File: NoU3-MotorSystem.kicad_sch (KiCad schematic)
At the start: 38 parts, among them J1 JST SR/SZ, J10 JST SR/SZ, J13 JST SR/SZ, J15 Barrel_Jack, J16 VIN, J17 JST SR/SZ, J18 GND, J4 JST SR/SZ, J7 JST SR/SZ, Q1 AO3401A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

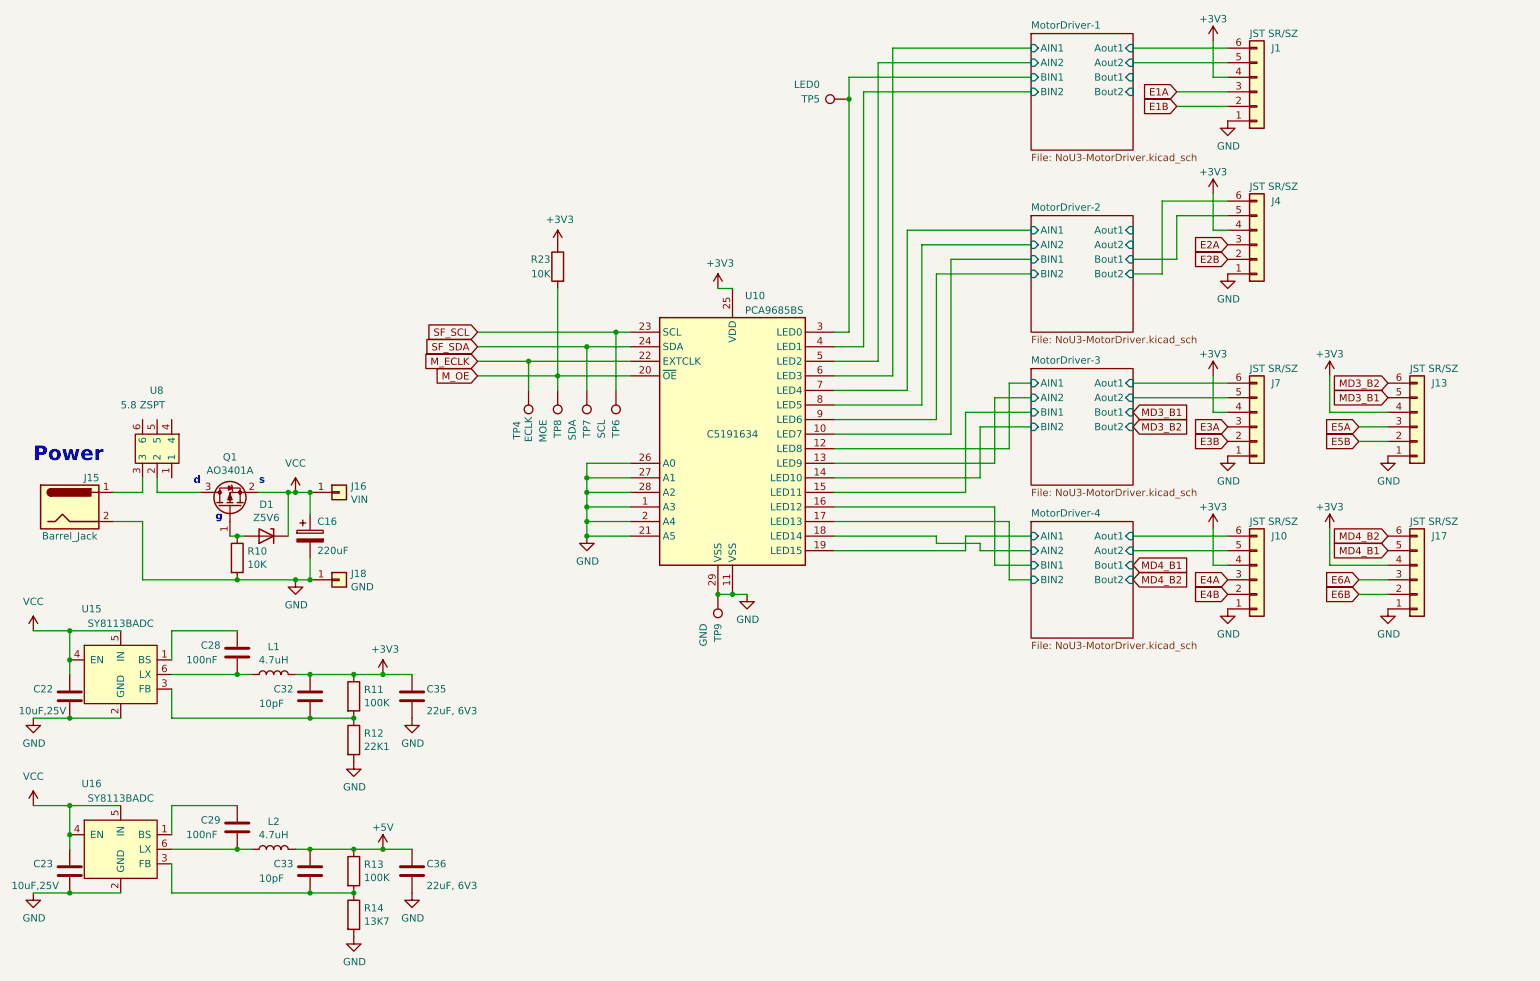
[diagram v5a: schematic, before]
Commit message: added 7th encoder, 2nd 220uf cap
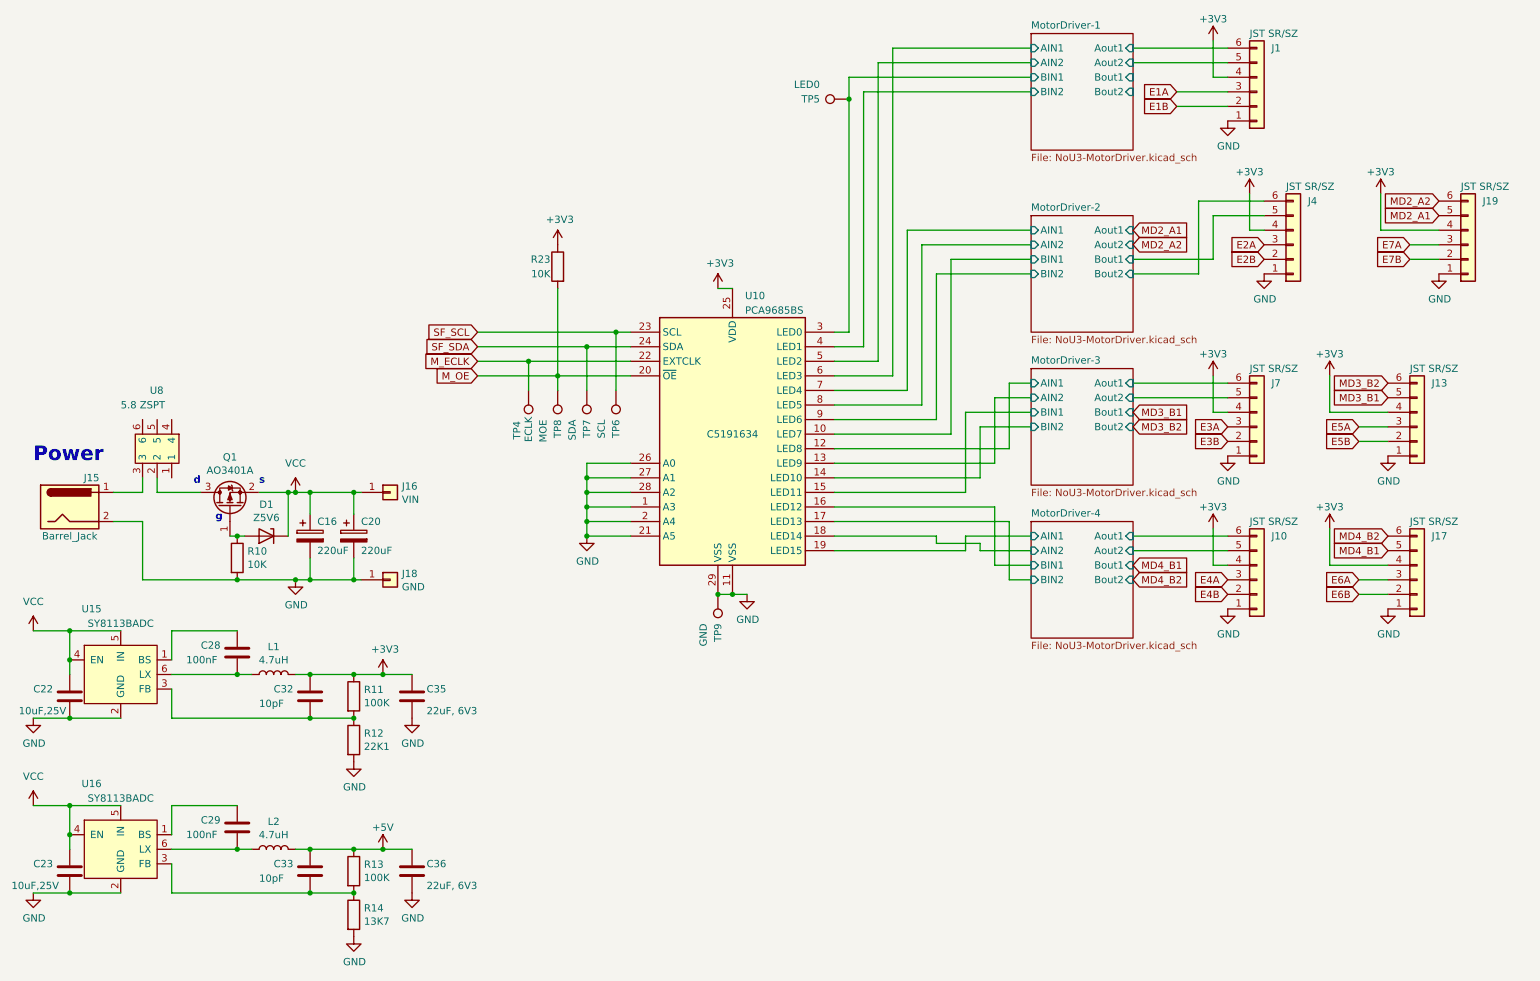
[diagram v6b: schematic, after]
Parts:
- added C20: 220uF, Capacitor_SMD:CP_Elec_6.3x7.7, symbol Device:C_Polarized
- added J19: JST SR/SZ, AlfredoFootprints:JST_SH_1x06_Vertical, symbol Connector_Generic:Conn_01x06
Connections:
- net +3V3: now also J19.4 (Pin_4)
- net GND: now also C20.2, J19.1 (Pin_1)
- net VCC: now also C20.1
- new net E7A: J19.3 (Pin_3)
- new net E7B: J19.2 (Pin_2)
- new net MD2_A1: J19.5 (Pin_5)
- new net MD2_A2: J19.6 (Pin_6)
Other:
- moved on the sheet: J16, J18, J4

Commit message: NoU3.5s as ordered 11/6/25
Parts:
- J7: LCSC C160392 -> C3029336
- R11: LCSC (none) -> C25741
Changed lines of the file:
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@@
 			)
 		)
-		(property "Datasheet" "https://jlcpcb.com/partdetail/171772-BM06B_SRSS_TB_LF_SN/C160392"
+		(property "Datasheet" ""
 			(at 237.49 97.79 0)
 			(effects
@@
 			)
 		)
-		(property "LCSC" "C160392"
+		(property "LCSC" "C3029336"
 			(at 237.49 97.79 0)
 			(effects
@@
 			)
 		)
-		(property "LCSC" ""
+		(property "LCSC" "C25741"
 			(at 80.01 144.78 0)
 			(effects

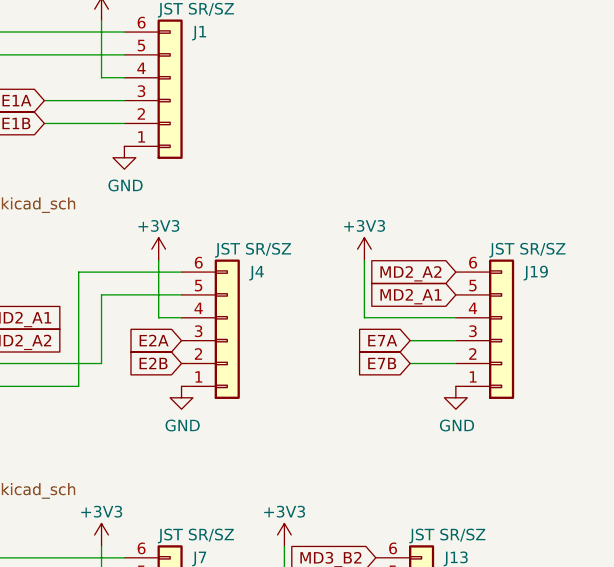
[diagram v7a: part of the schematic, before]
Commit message: Swap positions of MD2_A1 and MD2_A2 labels
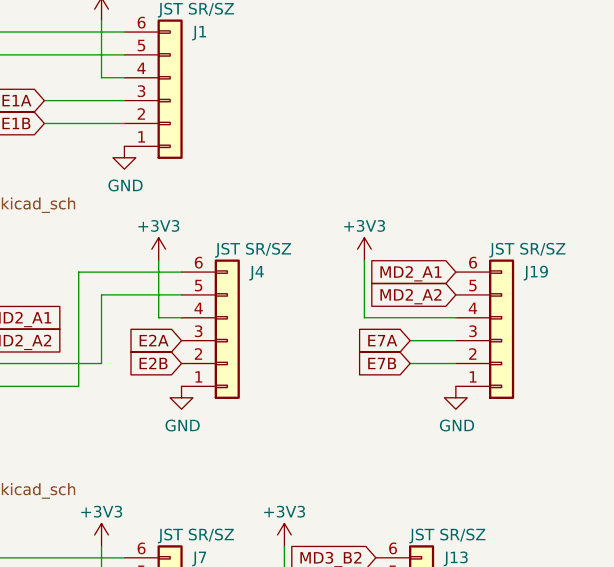
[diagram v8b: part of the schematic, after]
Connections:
- net MD2_A1: now also J19.6 (Pin_6); no longer J19.5 (Pin_5)
- net MD2_A2: now also J19.5 (Pin_5); no longer J19.6 (Pin_6)
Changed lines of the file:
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@@
 	(global_label "MD2_A2"
 		(shape input)
+		(at 269.24 60.96 180)
+		(fields_autoplaced yes)
+		(effects
+			(font
+				(size 1.27 1.27)
+			)
+			(justify right)
+		)
+		(property "Intersheetrefs" "${INTERSHEET_REFS}"
+			(at 259.7124 60.96 0)
+			(effects
+				(font
+					(size 1.27 1.27)
+				)
+				(justify right)
+				(hide yes)
+			)
+		)
+	)
+	(global_label "E6B"
+		(shape input)
+		(at 255.27 127 180)
+		(fields_autoplaced yes)
+		(effects
+			(font
+				(size 1.27 1.27)
+			)
+			(justify right)
+		)
+		(property "Intersheetrefs" "${INTERSHEET_REFS}"
+			(at 249.3899 127 0)
+			(effects
+				(font
+					(size 1.27 1.27)
+				)
+				(justify right)
+				(hide yes)
+			)
+		)
+	)
+	(global_label "MD3_B1"
+		(shape input)
+		(at 215.9 95.25 0)
+		(fields_autoplaced yes)
+		(effects
+			(font
+				(size 1.27 1.27)
+			)
+			(justify left)
+		)
+		(property "Intersheetrefs" "${INTERSHEET_REFS}"
+			(at 225.5296 95.25 0)
+			(effects
+				(font
+					(size 1.27 1.27)
+				)
+				(justify left)
+				(hide yes)
+			)
+		)
+	)
+	(global_label "MD3_B1"
+		(shape input)
+		(at 260.35 92.71 180)
+		(fields_autoplaced yes)
+		(effects
+			(font
+				(size 1.27 1.27)
+			)
+			(justify right)
+		)
+		(property "Intersheetrefs" "${INTERSHEET_REFS}"
+			(at 250.7204 92.71 0)
+			(effects
+				(font
+					(size 1.27 1.27)
+				)
+				(justify right)
+				(hide yes)
+			)
+		)
+	)
+	(global_label "MD2_A1"
+		(shape input)
+		(at 215.9 63.5 0)
+		(fields_autoplaced yes)
+		(effects
+			(font
+				(size 1.27 1.27)
+			)
+			(justify left)
+		)
+		(property "Intersheetrefs" "${INTERSHEET_REFS}"
+			(at 225.4276 63.5 0)
+			(effects
+				(font
+					(size 1.27 1.27)
+				)
+				(justify left)
+				(hide yes)
+			)
+		)
+	)
+	(global_label "E7B"
+		(shape input)
+		(at 264.16 68.58 180)
+		(fields_autoplaced yes)
+		(effects
+			(font
+				(size 1.27 1.27)
+			)
+			(justify right)
+		)
+		(property "Intersheetrefs" "${INTERSHEET_REFS}"
+			(at 258.2005 68.58 0)
+			(effects
+				(font
+					(size 1.27 1.27)
+				)
+				(justify right)
+				(hide yes)
+			)
+		)
+	)
+	(global_label "E5A"
+		(shape input)
+		(at 255.27 97.79 180)
+		(fields_autoplaced yes)
+		(effects
+			(font
+				(size 1.27 1.27)
+			)
+			(justify right)
+		)
+		(property "Intersheetrefs" "${INTERSHEET_REFS}"
+			(at 249.5713 97.79 0)
+			(effects
+				(font
+					(size 1.27 1.27)
+				)
+				(justify right)
+				(hide yes)
+			)
+		)
+	)
+	(global_label "E3B"
+		(shape input)
+		(at 232.41 100.33 180)
+		(fields_autoplaced yes)
+		(effects
+			(font
+				(size 1.27 1.27)
+			)
+			(justify right)
+		)
+		(property "Intersheetrefs" "${INTERSHEET_REFS}"
+			(at 226.5299 100.33 0)
+			(effects
+				(font
+					(size 1.27 1.27)
+				)
+				(justify right)
+				(hide yes)
+			)
+		)
+	)
+	(global_label "E7A"
+		(shape input)
+		(at 264.16 66.04 180)
+		(fields_autoplaced yes)
+		(effects
+			(font
+				(size 1.27 1.27)
+			)
+			(justify right)
+		)
+		(property "Intersheetrefs" "${INTERSHEET_REFS}"
+			(at 258.3819 66.04 0)
+			(effects
+				(font
+					(size 1.27 1.27)
+				)
+				(justify right)
+				(hide yes)
+			)
+		)
+	)
+	(global_label "M_ECLK"
+		(shape input)
+		(at 101.6 86.36 180)
+		(fields_autoplaced yes)
+		(effects
+			(font
+				(size 1.27 1.27)
+			)
+			(justify right)
+		)
+		(property "Intersheetrefs" "${INTERSHEET_REFS}"
+			(at 92.1329 86.36 0)
+			(effects
+				(font
+					(size 1.27 1.27)
+				)
+				(justify right)
+				(hide yes)
+			)
+		)
+	)
+	(global_label "M_OE"
+		(shape input)
+		(at 101.6 88.9 180)
+		(fields_autoplaced yes)
+		(effects
+			(font
+				(size 1.27 1.27)
+			)
+			(justify right)
+		)
+		(property "Intersheetrefs" "${INTERSHEET_REFS}"
+			(at 94.3705 88.9 0)
+			(effects
+				(font
+					(size 1.27 1.27)
+				)
+				(justify right)
+				(hide yes)
+			)
+		)
+	)
+	(global_label "MD2_A1"
+		(shape input)
 		(at 269.24 58.42 180)
 		(fields_autoplaced yes)
@@
 			(effects
 				(font
-					(size 1.27 1.27)
-				)
-				(justify right)
-				(hide yes)
-			)
-		)
-	)
-	(global_label "E6B"
-		(shape input)
-		(at 255.27 127 180)
-		(fields_autoplaced yes)
-		(effects
-			(font
-				(size 1.27 1.27)
-			)
-			(justify right)
-		)
-		(property "Intersheetrefs" "${INTERSHEET_REFS}"
-			(at 249.3899 127 0)
-			(effects
-				(font
-					(size 1.27 1.27)
-				)
-				(justify right)
-				(hide yes)
-			)
-		)
-	)
-	(global_label "MD3_B1"
-		(shape input)
-		(at 215.9 95.25 0)
-		(fields_autoplaced yes)
-		(effects
-			(font
-				(size 1.27 1.27)
-			)
-			(justify left)
-		)
-		(property "Intersheetrefs" "${INTERSHEET_REFS}"
-			(at 225.5296 95.25 0)
-			(effects
-				(font
-					(size 1.27 1.27)
-				)
-				(justify left)
-				(hide yes)
-			)
-		)
-	)
-	(global_label "MD3_B1"
-		(shape input)
-		(at 260.35 92.71 180)
-		(fields_autoplaced yes)
-		(effects
-			(font
-				(size 1.27 1.27)
-			)
-			(justify right)
-		)
-		(property "Intersheetrefs" "${INTERSHEET_REFS}"
-			(at 250.7204 92.71 0)
-			(effects
-				(font
-					(size 1.27 1.27)
-				)
-				(justify right)
-				(hide yes)
-			)
-		)
-	)
-	(global_label "MD2_A1"
-		(shape input)
-		(at 215.9 63.5 0)
-		(fields_autoplaced yes)
-		(effects
-			(font
-				(size 1.27 1.27)
-			)
-			(justify left)
-		)
-		(property "Intersheetrefs" "${INTERSHEET_REFS}"
-			(at 225.4276 63.5 0)
-			(effects
-				(font
-					(size 1.27 1.27)
-				)
-				(justify left)
-				(hide yes)
-			)
-		)
-	)
-	(global_label "E7B"
-		(shape input)
-		(at 264.16 68.58 180)
-		(fields_autoplaced yes)
-		(effects
-			(font
-				(size 1.27 1.27)
-			)
-			(justify right)
-		)
-		(property "Intersheetrefs" "${INTERSHEET_REFS}"
-			(at 258.2005 68.58 0)
-			(effects
-				(font
-					(size 1.27 1.27)
-				)
-				(justify right)
-				(hide yes)
-			)
-		)
-	)
-	(global_label "E5A"
-		(shape input)
-		(at 255.27 97.79 180)
-		(fields_autoplaced yes)
-		(effects
-			(font
-				(size 1.27 1.27)
-			)
-			(justify right)
-		)
-		(property "Intersheetrefs" "${INTERSHEET_REFS}"
-			(at 249.5713 97.79 0)
-			(effects
-				(font
-					(size 1.27 1.27)
-				)
-				(justify right)
-				(hide yes)
-			)
-		)
-	)
-	(global_label "E3B"
-		(shape input)
-		(at 232.41 100.33 180)
-		(fields_autoplaced yes)
-		(effects
-			(font
-				(size 1.27 1.27)
-			)
-			(justify right)
-		)
-		(property "Intersheetrefs" "${INTERSHEET_REFS}"
-			(at 226.5299 100.33 0)
-			(effects
-				(font
-					(size 1.27 1.27)
-				)
-				(justify right)
-				(hide yes)
-			)
-		)
-	)
-	(global_label "E7A"
-		(shape input)
-		(at 264.16 66.04 180)
-		(fields_autoplaced yes)
-		(effects
-			(font
-				(size 1.27 1.27)
-			)
-			(justify right)
-		)
-		(property "Intersheetrefs" "${INTERSHEET_REFS}"
-			(at 258.3819 66.04 0)
-			(effects
-				(font
-					(size 1.27 1.27)
-				)
-				(justify right)
-				(hide yes)
-			)
-		)
-	)
-	(global_label "M_ECLK"
-		(shape input)
-		(at 101.6 86.36 180)
-		(fields_autoplaced yes)
-		(effects
-			(font
-				(size 1.27 1.27)
-			)
-			(justify right)
-		)
-		(property "Intersheetrefs" "${INTERSHEET_REFS}"
-			(at 92.1329 86.36 0)
-			(effects
-				(font
-					(size 1.27 1.27)
-				)
-				(justify right)
-				(hide yes)
-			)
-		)
-	)
-	(global_label "M_OE"
-		(shape input)
-		(at 101.6 88.9 180)
-		(fields_autoplaced yes)
-		(effects
-			(font
-				(size 1.27 1.27)
-			)
-			(justify right)
-		)
-		(property "Intersheetrefs" "${INTERSHEET_REFS}"
-			(at 94.3705 88.9 0)
-			(effects
-				(font
-					(size 1.27 1.27)
-				)
-				(justify right)
-				(hide yes)
-			)
-		)
-	)
-	(global_label "MD2_A1"
-		(shape input)
-		(at 269.24 60.96 180)
-		(fields_autoplaced yes)
-		(effects
-			(font
-				(size 1.27 1.27)
-			)
-			(justify right)
-		)
-		(property "Intersheetrefs" "${INTERSHEET_REFS}"
-			(at 259.7124 60.96 0)
-			(effects
-				(font
